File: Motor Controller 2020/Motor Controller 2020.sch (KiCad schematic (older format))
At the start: 37 parts, among them J1 Batt+, J2 Batt-, J3 Input, J4 Motor+, J5 Motor-, Q1 IRF1404, Q2 IRF1404, Q3 IRF1404, Q4 IRF1404, Q5 IRF1404, Q6 IRF1404, Q7 IRF1404, Q8 IRF1404, SW1 SW_DIP_x03, U1 L7805, U2 a4956, U3 Attiny4313

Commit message: Added reset/program jumper to board
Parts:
- added JP3: Program/Reset, Connector_PinHeader_2.54mm:PinHeader_1x02_P2.54mm_Vertical_SMD_Pin1Right, symbol Device:Jumper_NO_Small
- U2: symbol Created_Components:a4956 -> Motor-Controller-2020-rescue:a4956-Created_Components
- U3: symbol Created_Components:Attiny4313 -> Motor-Controller-2020-rescue:Attiny4313-Created_Components
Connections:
- wire segments 187 -> 192
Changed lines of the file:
@@
 Connection ~ 1050 1000
 $Comp
-L Created_Components:Attiny4313 U3
+L Motor-Controller-2020-rescue:Attiny4313-Created_Components U3
 U 1 1 60BC11AB
 P 2450 4200
@@
 L power:+5V #PWR013
 U 1 1 60BC4BAD
-P 2350 3450
-F 0 "#PWR013" H 2350 3300 50  0001 C CNN
-F 1 "+5V" H 2350 3600 50  0000 C CNN
-F 2 "" H 2350 3450 50  0001 C CNN
-F 3 "" H 2350 3450 50  0001 C CNN
-	1    2350 3450
+P 2350 3300
+F 0 "#PWR013" H 2350 3150 50  0001 C CNN
+F 1 "+5V" H 2350 3450 50  0000 C CNN
+F 2 "" H 2350 3300 50  0001 C CNN
+F 3 "" H 2350 3300 50  0001 C CNN
+	1    2350 3300
 	1    0    0    -1
 $EndComp
@@
 	1    0    0    -1
 $EndComp
-Wire Wire Line
-	2350 3450 2350 3550
 Wire Wire Line
 	2200 3550 2350 3550
@@
 Wire Wire Line
 	950  3300 1050 3300
-Text GLabel 2550 3550 1    50   Input ~ 0
+Text GLabel 3050 3550 2    50   Input ~ 0
 A_RESET
-Wire Wire Line
-	2550 3550 2550 3750
-$Comp
-L Created_Components:a4956 U2
+$Comp
+L Motor-Controller-2020-rescue:a4956-Created_Components U2
 U 1 1 60B5A6BA
 P 8550 4100
@@
 Wire Wire Line
 	7850 4150 8000 4150
+$Comp
+L Device:Jumper_NO_Small JP3
+U 1 1 60CC469F
+P 2600 3550
+F 0 "JP3" H 2600 3365 50  0000 C CNN
+F 1 "Program/Reset" H 2550 3450 50  0000 C CNN
+F 2 "Connector_PinHeader_2.54mm:PinHeader_1x02_P2.54mm_Vertical_SMD_Pin1Right" H 2600 3550 50  0001 C CNN
+F 3 "~" H 2600 3550 50  0001 C CNN
+	1    2600 3550
+	-1   0    0    1
+$EndComp
+Wire Wire Line
+	2350 3300 2350 3550
+Wire Wire Line
+	2550 3750 2550 3650
+Wire Wire Line
+	2550 3650 2850 3650
+Wire Wire Line
+	2850 3650 2850 3550
+Wire Wire Line
+	2850 3550 3050 3550
+Wire Wire Line
+	2350 3550 2500 3550
+Wire Wire Line
+	2700 3550 2850 3550
+Connection ~ 2850 3550
 $EndSCHEMATC

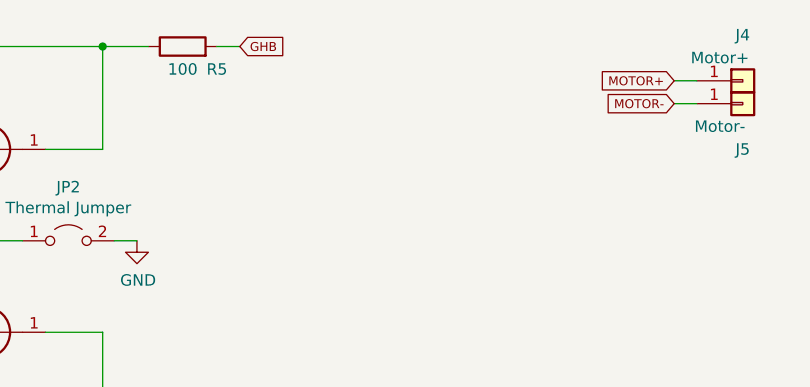
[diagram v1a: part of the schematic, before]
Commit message: Added mounting holes instead of trying to slide the board into the housing
The 3D printed slide mechanism didn't work because the printer couldn't reproduce the sharp corners
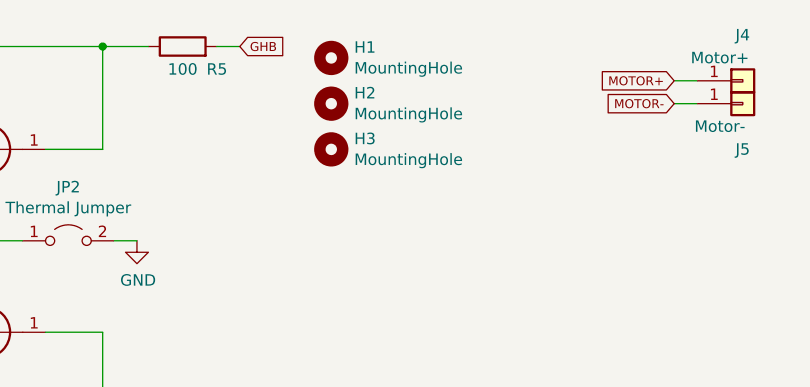
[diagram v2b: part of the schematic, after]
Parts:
- added H1, H2, H3: MountingHole, MountingHole:MountingHole_3.2mm_M3, symbol Mechanical:MountingHole
- JP3: footprint Connector_PinHeader_2.54mm:PinHeader_1x02_P2.54mm_Vertical_SMD_Pin1Right -> Connector_PinHeader_2.54mm:PinHeader_1x02_P2.54mm_Horizontal
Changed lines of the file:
@@
 U 1 1 60CC469F
 P 2600 3550
-F 0 "JP3" H 2600 3365 50  0000 C CNN
-F 1 "Program/Reset" H 2550 3450 50  0000 C CNN
-F 2 "Connector_PinHeader_2.54mm:PinHeader_1x02_P2.54mm_Vertical_SMD_Pin1Right" H 2600 3550 50  0001 C CNN
+F 0 "JP3" H 2600 3650 50  0000 C CNN
+F 1 "Program/Reset" H 2650 3600 50  0000 C CNN
+F 2 "Connector_PinHeader_2.54mm:PinHeader_1x02_P2.54mm_Horizontal" H 2600 3550 50  0001 C CNN
 F 3 "~" H 2600 3550 50  0001 C CNN
 	1    2600 3550
-	-1   0    0    1
+	1    0    0    -1
 $EndComp
 Wire Wire Line
@@
 	2700 3550 2850 3550
 Connection ~ 2850 3550
+$Comp
+L Mechanical:MountingHole H1
+U 1 1 60CD765C
+P 8500 700
+F 0 "H1" H 8600 746 50  0000 L CNN
+F 1 "MountingHole" H 8600 655 50  0000 L CNN
+F 2 "MountingHole:MountingHole_3.2mm_M3" H 8500 700 50  0001 C CNN
+F 3 "~" H 8500 700 50  0001 C CNN
+	1    8500 700
+	1    0    0    -1
+$EndComp
+$Comp
+L Mechanical:MountingHole H2
+U 1 1 60CD840C
+P 8500 900
+F 0 "H2" H 8600 946 50  0000 L CNN
+F 1 "MountingHole" H 8600 855 50  0000 L CNN
+F 2 "MountingHole:MountingHole_3.2mm_M3" H 8500 900 50  0001 C CNN
+F 3 "~" H 8500 900 50  0001 C CNN
+	1    8500 900
+	1    0    0    -1
+$EndComp
+$Comp
+L Mechanical:MountingHole H3
+U 1 1 60CD8691
+P 8500 1100
+F 0 "H3" H 8600 1146 50  0000 L CNN
+F 1 "MountingHole" H 8600 1055 50  0000 L CNN
+F 2 "MountingHole:MountingHole_3.2mm_M3" H 8500 1100 50  0001 C CNN
+F 3 "~" H 8500 1100 50  0001 C CNN
+	1    8500 1100
+	1    0    0    -1
+$EndComp
 $EndSCHEMATC

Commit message: Fixed driver reset bugs
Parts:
- removed JP3: Program/Reset, Connector_PinHeader_2.54mm:PinHeader_1x02_P2.54mm_Horizontal, symbol Device:Jumper_NO_Small
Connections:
- wire segments 192 -> 187
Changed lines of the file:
@@
 Wire Wire Line
 	950  3300 1050 3300
-Text GLabel 3050 3550 2    50   Input ~ 0
+Text GLabel 2550 3650 1    50   Input ~ 0
 A_RESET
 $Comp
@@
 Wire Wire Line
 	7850 4150 8000 4150
-$Comp
-L Device:Jumper_NO_Small JP3
-U 1 1 60CC469F
-P 2600 3550
-F 0 "JP3" H 2600 3650 50  0000 C CNN
-F 1 "Program/Reset" H 2650 3600 50  0000 C CNN
-F 2 "Connector_PinHeader_2.54mm:PinHeader_1x02_P2.54mm_Horizontal" H 2600 3550 50  0001 C CNN
-F 3 "~" H 2600 3550 50  0001 C CNN
-	1    2600 3550
-	1    0    0    -1
-$EndComp
 Wire Wire Line
 	2350 3300 2350 3550
 Wire Wire Line
 	2550 3750 2550 3650
-Wire Wire Line
-	2550 3650 2850 3650
-Wire Wire Line
-	2850 3650 2850 3550
-Wire Wire Line
-	2850 3550 3050 3550
-Wire Wire Line
-	2350 3550 2500 3550
-Wire Wire Line
-	2700 3550 2850 3550
-Connection ~ 2850 3550
 $Comp
 L Mechanical:MountingHole H1

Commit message: Add files via upload
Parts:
- removed U1: L7805, Package_TO_SOT_SMD:SOT-223, symbol Regulator_Linear:L7805
- added C7: 1uF, Capacitor_SMD:C_1210_3225Metric, symbol Device:C
- added L1: 47uH, Inductor_SMD:L_1210_3225Metric, symbol pspice:INDUCTOR
- added U1: MAX15062A, Package_DFN_QFN:DFN-8_2x2mm_P0.5mm, symbol Regulator_Switching:MAX15062A
- C1: value 0.33uF -> 1uF; footprint Capacitor_SMD:C_1812_4532Metric_Pad1.57x3.40mm_HandSolder -> Capacitor_SMD:C_1210_3225Metric
- C2: value 0.1uF -> 10uF; footprint Capacitor_SMD:C_1812_4532Metric_Pad1.57x3.40mm_HandSolder -> Capacitor_SMD:C_1210_3225Metric
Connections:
- net +12V: now also U1.1 (VIN), U1.2 (EN/UVLO)
- net +5V: now also L1.2, U1.4 (FB/Vout)
- net GND: now also C7.2, U1.7 (GND)
- new net: C7.1, U1.3 (VCC)
- no-connect marks 8 -> 10
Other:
- note added: "System can operate from 12-48V"
- moved on the sheet: H1, H2, H3, JP1, JP2, Q1, Q2, Q3, Q4, Q5, Q6, Q7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

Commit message: Add files via upload
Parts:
- Q1, Q2, Q3, Q4, Q5, Q6, Q7, Q8: footprint Package_TO_SOT_SMD:TO-263-3_TabPin2 -> Package_TO_SOT_SMD:TO-263-2
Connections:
- net at L1.1: now also U1.8 (LX)
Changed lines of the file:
@@
 F 0 "Q7" H 7755 1146 50  0000 L CNN
 F 1 "IRF1404" H 7755 1055 50  0000 L CNN
-F 2 "Package_TO_SOT_SMD:TO-263-3_TabPin2" H 7550 1100 50  0001 C CIN
+F 2 "Package_TO_SOT_SMD:TO-263-2" H 7550 1100 50  0001 C CIN
 F 3 "https://www.infineon.com/dgdl/Infineon-IRF40DM229-DS-v02_00-EN.pdf?fileId=5546d462557e6e890155a15c899160ea" H 7550 1100 50  0001 L CNN
 F 4 "M" H 7550 1100 50  0001 C CNN "Spice_Primitive"
@@
 F 0 "Q6" H 8505 1146 50  0000 L CNN
 F 1 "IRF1404" H 8505 1055 50  0000 L CNN
-F 2 "Package_TO_SOT_SMD:TO-263-3_TabPin2" H 8300 1100 50  0001 C CIN
+F 2 "Package_TO_SOT_SMD:TO-263-2" H 8300 1100 50  0001 C CIN
 F 3 "https://www.infineon.com/dgdl/Infineon-IRF40DM229-DS-v02_00-EN.pdf?fileId=5546d462557e6e890155a15c899160ea" H 8300 1100 50  0001 L CNN
 F 4 "M" H 8300 1100 50  0001 C CNN "Spice_Primitive"
@@
 F 0 "Q3" H 6205 1146 50  0000 L CNN
 F 1 "IRF1404" H 6205 1055 50  0000 L CNN
-F 2 "Package_TO_SOT_SMD:TO-263-3_TabPin2" H 6000 1100 50  0001 C CIN
+F 2 "Package_TO_SOT_SMD:TO-263-2" H 6000 1100 50  0001 C CIN
 F 3 "https://www.infineon.com/dgdl/Infineon-IRF40DM229-DS-v02_00-EN.pdf?fileId=5546d462557e6e890155a15c899160ea" H 6000 1100 50  0001 L CNN
 F 4 "M" H 6000 1100 50  0001 C CNN "Spice_Primitive"
@@
 F 0 "Q1" H 5455 1146 50  0000 L CNN
 F 1 "IRF1404" H 5455 1055 50  0000 L CNN
-F 2 "Package_TO_SOT_SMD:TO-263-3_TabPin2" H 5250 1100 50  0001 C CIN
+F 2 "Package_TO_SOT_SMD:TO-263-2" H 5250 1100 50  0001 C CIN
 F 3 "https://www.infineon.com/dgdl/Infineon-IRF40DM229-DS-v02_00-EN.pdf?fileId=5546d462557e6e890155a15c899160ea" H 5250 1100 50  0001 L CNN
 F 4 "M" H 5250 1100 50  0001 C CNN "Spice_Primitive"
@@
 F 0 "Q2" H 5455 1946 50  0000 L CNN
 F 1 "IRF1404" H 5455 1855 50  0000 L CNN
-F 2 "Package_TO_SOT_SMD:TO-263-3_TabPin2" H 5250 1900 50  0001 C CIN
+F 2 "Package_TO_SOT_SMD:TO-263-2" H 5250 1900 50  0001 C CIN
 F 3 "https://www.infineon.com/dgdl/Infineon-IRF40DM229-DS-v02_00-EN.pdf?fileId=5546d462557e6e890155a15c899160ea" H 5250 1900 50  0001 L CNN
 F 4 "M" H 5250 1900 50  0001 C CNN "Spice_Primitive"
@@
 F 0 "Q4" H 6205 1946 50  0000 L CNN
 F 1 "IRF1404" H 6205 1855 50  0000 L CNN
-F 2 "Package_TO_SOT_SMD:TO-263-3_TabPin2" H 6000 1900 50  0001 C CIN
+F 2 "Package_TO_SOT_SMD:TO-263-2" H 6000 1900 50  0001 C CIN
 F 3 "https://www.infineon.com/dgdl/Infineon-IRF40DM229-DS-v02_00-EN.pdf?fileId=5546d462557e6e890155a15c899160ea" H 6000 1900 50  0001 L CNN
 F 4 "M" H 6000 1900 50  0001 C CNN "Spice_Primitive"
@@
 F 0 "Q5" H 7755 1946 50  0000 L CNN
 F 1 "IRF1404" H 7755 1855 50  0000 L CNN
-F 2 "Package_TO_SOT_SMD:TO-263-3_TabPin2" H 7550 1900 50  0001 C CIN
+F 2 "Package_TO_SOT_SMD:TO-263-2" H 7550 1900 50  0001 C CIN
 F 3 "https://www.infineon.com/dgdl/Infineon-IRF40DM229-DS-v02_00-EN.pdf?fileId=5546d462557e6e890155a15c899160ea" H 7550 1900 50  0001 L CNN
 F 4 "M" H 7550 1900 50  0001 C CNN "Spice_Primitive"
@@
 F 0 "Q8" H 8505 1946 50  0000 L CNN
 F 1 "IRF1404" H 8505 1855 50  0000 L CNN
-F 2 "Package_TO_SOT_SMD:TO-263-3_TabPin2" H 8300 1900 50  0001 C CIN
+F 2 "Package_TO_SOT_SMD:TO-263-2" H 8300 1900 50  0001 C CIN
 F 3 "https://www.infineon.com/dgdl/Infineon-IRF40DM229-DS-v02_00-EN.pdf?fileId=5546d462557e6e890155a15c899160ea" H 8300 1900 50  0001 L CNN
 F 4 "M" H 8300 1900 50  0001 C CNN "Spice_Primitive"
@@
 Text Notes 1250 600  0    50   ~ 0
 System can operate from 12-48V
+Wire Wire Line
+	2050 1650 2100 1650
 $EndSCHEMATC

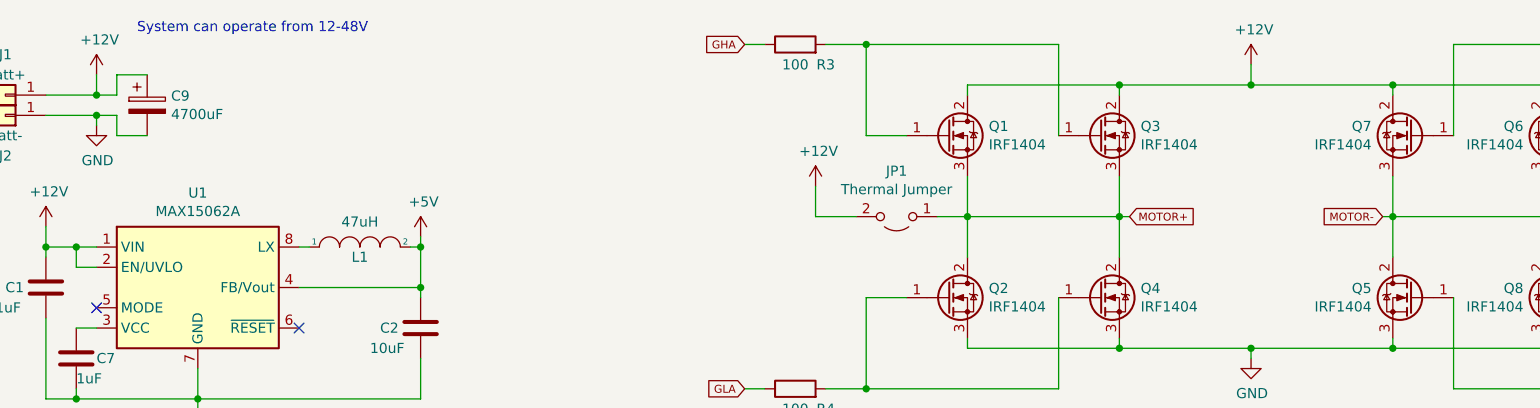
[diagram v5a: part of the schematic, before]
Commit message: Updated controller PCB
Added several capacitors to help with switching transients
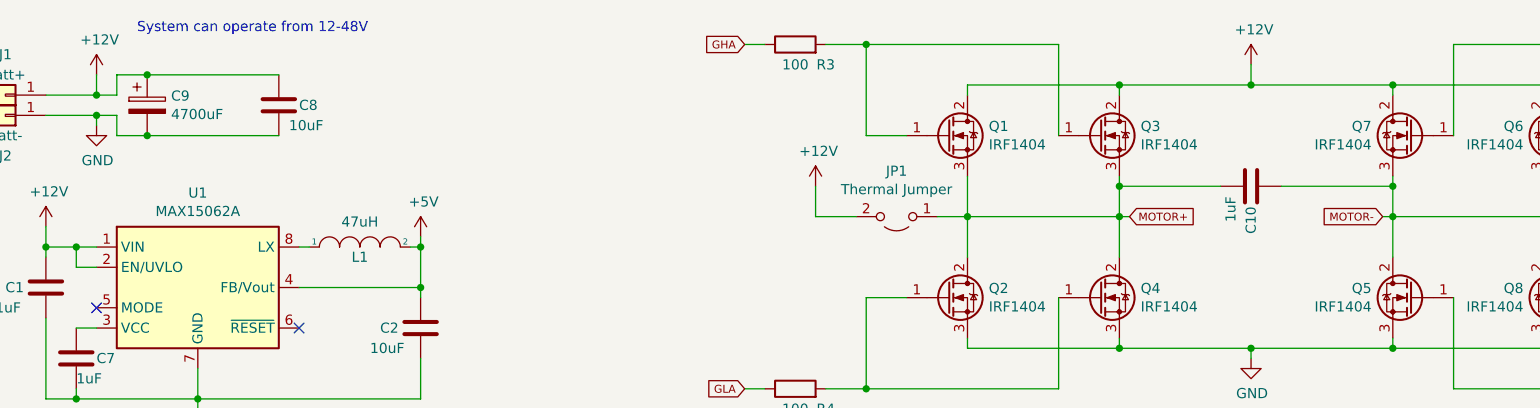
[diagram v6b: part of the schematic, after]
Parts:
- added C10: 1uF, Capacitor_THT:C_Disc_D5.0mm_W2.5mm_P2.50mm, symbol Device:C
- added C8: 10uF, Capacitor_SMD:C_1210_3225Metric, symbol Device:C
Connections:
- net +12V: now also C8.1
- net GND: now also C8.2
- net MOTOR+: now also C10.2
- net MOTOR-: now also C10.1
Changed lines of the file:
@@
 Connection ~ 6100 2150
 Wire Wire Line
-	7450 1300 7450 1500
+	7450 1300 7450 1350
 Wire Wire Line
 	8200 1300 8200 1500
 Wire Wire Line
-	6100 1300 6100 1500
+	6100 1300 6100 1350
 Wire Wire Line
 	5350 1300 5350 1500
@@
 Wire Wire Line
 	2050 1650 2100 1650
+$Comp
+L Device:C C8
+U 1 1 60DE7EE1
+P 1950 950
+F 0 "C8" H 2050 950 50  0000 L CNN
+F 1 "10uF" H 2000 850 50  0000 L CNN
+F 2 "Capacitor_SMD:C_1210_3225Metric" H 1988 800 50  0001 C CNN
+F 3 "~" H 1950 950 50  0001 C CNN
+	1    1950 950
+	1    0    0    -1
+$EndComp
+Wire Wire Line
+	1950 800  1300 800
+Connection ~ 1300 800
+Wire Wire Line
+	1950 1100 1300 1100
+Connection ~ 1300 1100
+$Comp
+L Device:C C10
+U 1 1 60DFEE39
+P 6750 1350
+F 0 "C10" H 6850 1350 50  0000 L CNN
+F 1 "1uF" H 6800 1250 50  0000 L CNN
+F 2 "Capacitor_THT:C_Disc_D5.0mm_W2.5mm_P2.50mm" H 6788 1200 50  0001 C CNN
+F 3 "~" H 6750 1350 50  0001 C CNN
+	1    6750 1350
+	0    1    1    0
+$EndComp
+Wire Wire Line
+	6900 1350 7450 1350
+Connection ~ 7450 1350
+Wire Wire Line
+	7450 1350 7450 1500
+Wire Wire Line
+	6600 1350 6100 1350
+Connection ~ 6100 1350
+Wire Wire Line
+	6100 1350 6100 1500
 $EndSCHEMATC
